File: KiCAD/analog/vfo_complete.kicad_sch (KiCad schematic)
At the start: 57 parts, among them J1 Filter Out, J10 Filter Out, J2 Filter Out, Q2 40673, U10 LM7171xIN, U11 LM7171xIN, U12 LM7171xIN, U5 Si5351A_Breakout

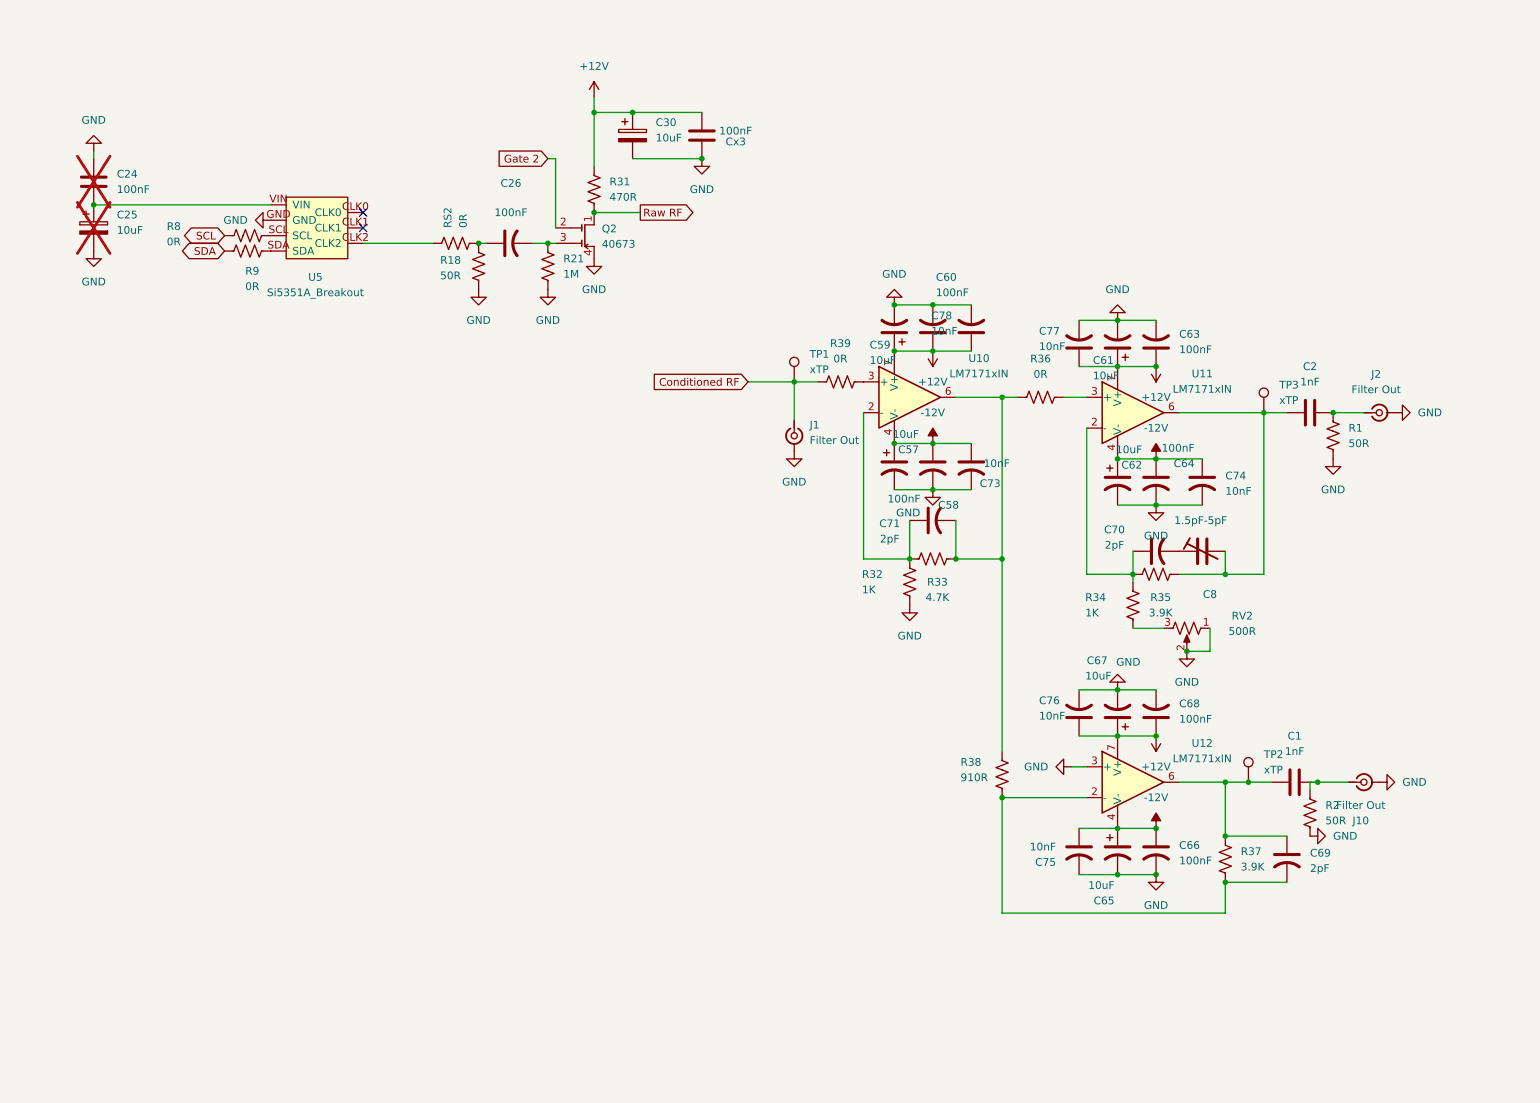
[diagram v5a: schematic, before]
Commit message: revD: analog board — DGFET+RC+buffer chain, LPF moved to ss_pa, PCB resized
Architecture change motivated by the Rev C sim finding that the LM7171
PP driver's +/-12V rails capped clean output at ~4.5W (see commit
3ce203d). Rev D delegates the gain-driver job to an external PA stage
(expected: QRP Labs 10W kit), so the analog board now just:
  Si5351 -> DGFET keyer -> R1(50)+C1(100p) RC @ 32MHz
         -> U1 LM7171 unity-gain follower -> R2(50) back-match -> J1 coax

Analog board changes (vfo_complete.kicad_sch):
  * DELETED: U10, U11, U12 (LM7171 PP driver chain) + feedback R/C,
    AC-coupling caps, V_BIAS network, R_GA/R_GB, C_GA/C_GB, J3/J4
    (dual-ended PP coax outputs)
  * DELETED: U2 reconstruction LPF stage (part of lpf.kicad_sch which
    is now emptied -- content moved to ss_pa/lpf.kicad_sch)
  * ADDED: R1=50R + C1=100pF (32 MHz single-pole RC snubber at the
    DGFET drain), U1 LM7171 unity-gain follower, R2=50R output
    back-match, J1 Conn_Coaxial_Small (new single-ended RF output),
    C2/C3=100nF op-amp bypass caps

Arduino sheet (arduino.kicad_sch):
  * ADDED: J2 Amphenol RJE1D-188 RJ45 for new external LPF board
    - Pins 1,2,3,6: RLY_10/15/17/20 band-select signals from PCF8575
    - Pins 5,8: GRID_CTL_A/B reserved spares for potential future
      tube PA (no other destination on the board, intentional)
    - Pins 4,7,SH: GND
  * ADDED: RLY_40 provision (not yet routed to J2, provision only)
  * T568B wire-pair arrangement for noise immunity

LPF content moved from analog/lpf.kicad_sch -> ss_pa/lpf.kicad_sch
(empty analog LPF sheet remains as a shell; delete later or repurpose).

PCB (analog.kicad_pcb):
  * Resized board outline from oversized 228x178 mm to 200x150 mm
    landscape (300 cm^2 / 46.5 in^2), centered on A3 at (210, 148.5)
  * Four M3 mounting holes H1-H4 placed 5 mm in from each corner
    (hole span 190 x 140 mm)
  * Added "board_only" attribute to each mounting hole so KiCad no
    longer flags them for deletion in Update PCB f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
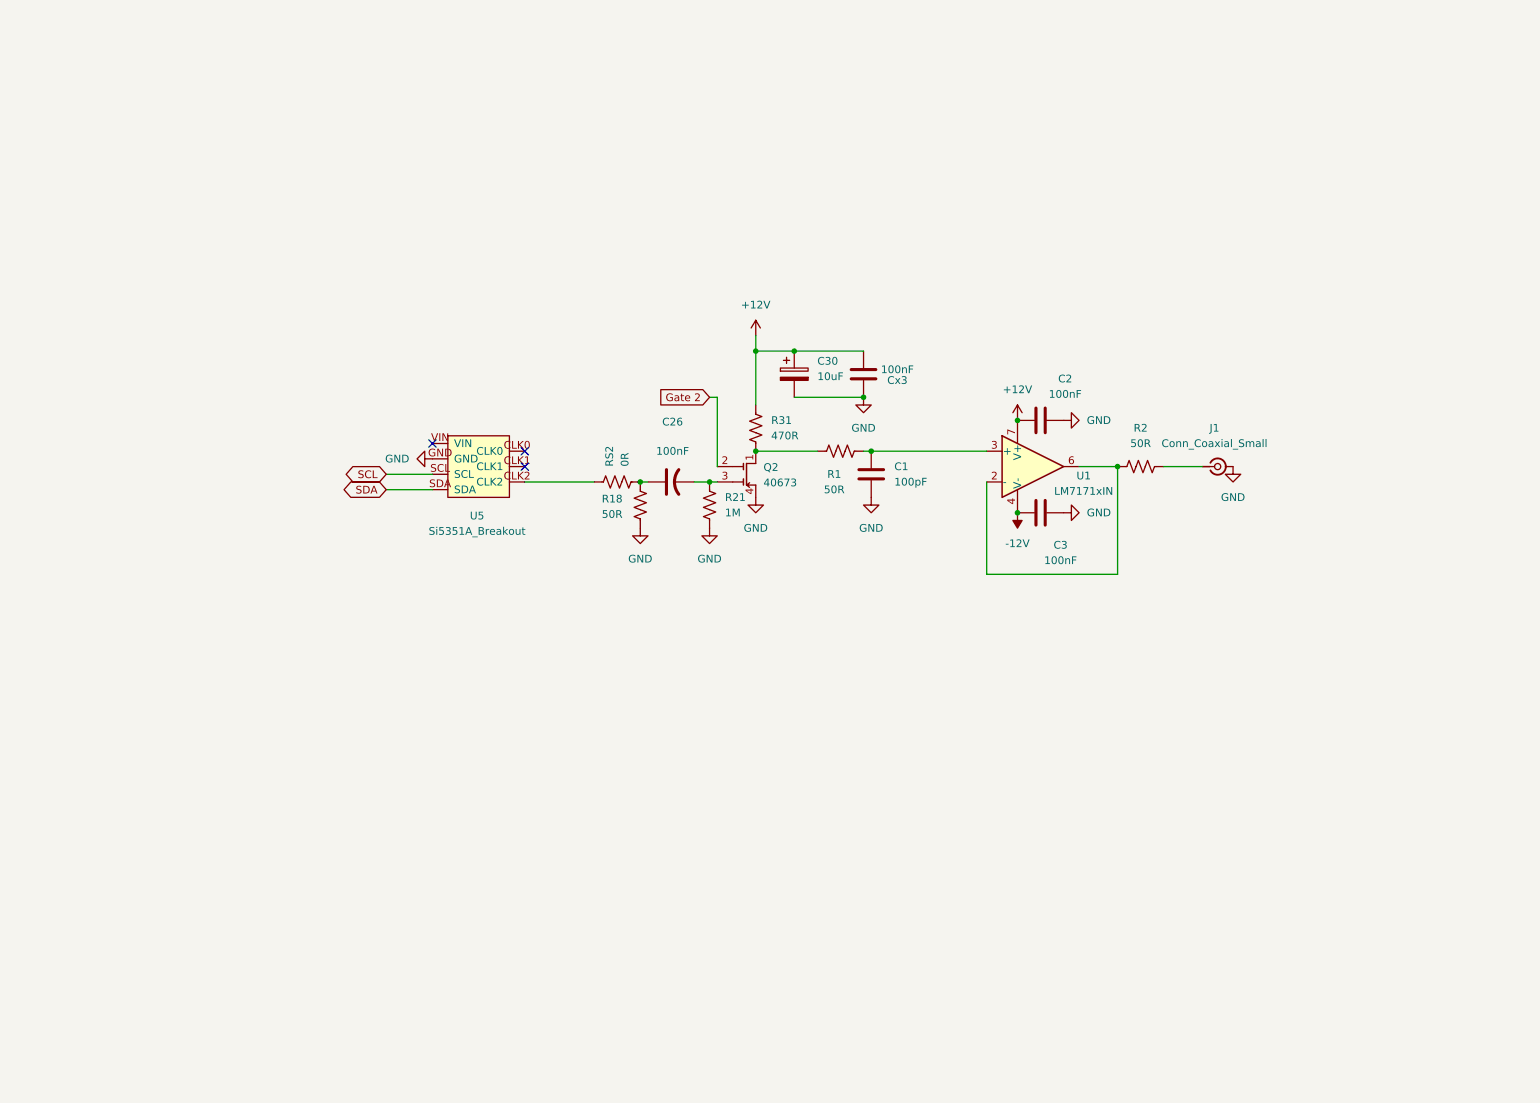
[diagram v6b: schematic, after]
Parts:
- removed C24: 100nF, Capacitor_THT:C_Disc_D5.0mm_W2.5mm_P5.00mm, symbol Device:C
- removed C25: 10uF, Capacitor_THT:CP_Radial_D5.0mm_P2.00mm, symbol Device:C_Polarized
- removed C57, C59, C61, C62, C65, C67: 10uF, Capacitor_THT:CP_Radial_D5.0mm_P2.00mm, symbol Device:C_Polarized_US
- removed C58, C60, C63, C64, C66, C68: 100nF, Capacitor_THT:C_Disc_D5.0mm_W2.5mm_P5.00mm, symbol Device:C_US
- removed C69, C70, C71: 2pF, xmitter:C_Axial_Kemet_Aximax_C41X_L4.5mm_D2.6mm_P7.62mm_Horizontal, symbol Device:C_US
- removed C73, C74, C75, C76, C77, C78: 10nF, Capacitor_THT:C_Disc_D6.0mm_W2.5mm_P5.00mm, symbol Device:C_US
- removed C8: 1.5pF-5pF, xmitter:Trimmer_Vishay_BFC2808_D5mm_P5.08mm, symbol Device:C_Trim
- removed J10, J2: Filter Out, Connector_Coaxial:SMA_Amphenol_132134_Vertical, symbol Connector:Conn_Coaxial_Small
- removed R32, R34: 1K, Resistor_THT:R_Axial_DIN0207_L6.3mm_D2.5mm_P10.16mm_Horizontal, symbol Device:R_US
- removed R33: 4.7K, Resistor_THT:R_Axial_DIN0207_L6.3mm_D2.5mm_P10.16mm_Horizontal, symbol Device:R_US
- removed R35, R37: 3.9K, Resistor_THT:R_Axial_DIN0207_L6.3mm_D2.5mm_P10.16mm_Horizontal, symbol Device:R_US
- removed R36, R39, R8, R9: 0R, Resistor_THT:R_Axial_DIN0207_L6.3mm_D2.5mm_P10.16mm_Horizontal, symbol Device:R_US
- removed R38: 910R, Resistor_THT:R_Axial_DIN0207_L6.3mm_D2.5mm_P10.16mm_Horizontal, symbol Device:R_US
- removed RV2: 500R, Potentiometer_THT:Potentiometer_Bourns_3296W_Vertical, symbol Device:R_Potentiometer_US
- removed TP1, TP2, TP3: xTP, Connector_PinHeader_2.54mm:PinHeader_1x01_P2.54mm_Vertical, symbol xmitter:xTP
- removed U10, U11, U12: LM7171xIN, Package_DIP:DIP-8_W7.62mm, symbol Amplifier_Operational:LM7171xIN
- added C3: 100nF, Capacitor_THT:C_Disc_D5.0mm_W2.5mm_P5.00mm, symbol Device:C
- added U1: LM7171xIN, Package_DIP:DIP-8_W7.62mm, symbol Amplifier_Operational:LM7171xIN
- C1: value 1nF -> 100pF
- C2: value 1nF -> 100nF; footprint Capacitor_THT:C_Rect_L7.0mm_W3.5mm_P5.00mm -> Capacitor_THT:C_Disc_D5.0mm_W2.5mm_P5.00mm
- J1: value Filter Out -> Conn_Coaxial_Small; footprint Connector_Coaxial:SMA_Amphenol_132134_Vertical -> xmitter:SMA_Cinch_142-0701-201_Vertical_JackPCB
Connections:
- net Raw RF is gone; now on an unnamed net: Q2.1 (D), R31.2
- net +12V: now also C2.1, U1.7 (V+)
- net -12V: now also C3.1, U1.4 (V-)
- net GND: now also C1.2, C2.2, C3.2; no longer R1.2, R2.2
- net SCL: now also U5.SCL
- net SDA: now also U5.SDA
- net at C1.1: now also R1.2, U1.3 (+)
- net at R2.1: now also U1.2 (-), U1.6; no longer C1.2
- net at R1.1: no longer C2.2
- net Conditioned RF: no longer names the net of J1.1 (In)
- net Conditioned RF: now also R2.2
- no-connect marks 2 -> 3
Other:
- moved on the sheet: C26, C30, Cx3, Q2, R18, R21, R31, RS2, U5

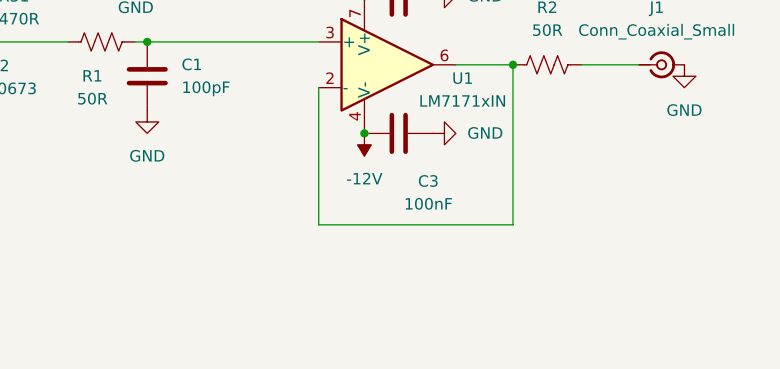
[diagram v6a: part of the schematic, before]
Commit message: revD analog: U1 gain hedge (R_f=3k installed, R_g unpopulated = unity default)
U1 (LM7171 buffer on analog) switched from unity-gain follower to a
non-inverting amplifier topology with a build-time gain hedge:

  - R_f = 3 kΩ installed in the feedback path (output -> inverting in)
  - R_g (inverting in -> GND) INTENTIONALLY LEFT UNPOPULATED by default

With R_g open, gain = 1 + R_f/R_g collapses to unity (nothing to force
current through R_f since LM7171 input bias is ~2 µA). Default signal
level at J1 is ~500 mVpp (unchanged from previous follower).

To get more drive at build time -- e.g. to push the IRF510 PA into
class-C operation when firmware sets PA_Bias_A/B low -- just populate
R_g with a value:
  R_g = 1 kΩ  -> gain = 4 -> ~2 Vpp into PA (comfortable, no clipping)
  R_g = 3 kΩ  -> gain = 2 -> ~1 Vpp
  R_g = 333 Ω -> gain = 10 -> clips, don't do

Amplitude control remains via Q2 (40673 DGFET) G2 driven by MCP4921
U4 ch A (envelope DAC via Q11/Q12 KeyUp mute level shifter). G2 acts
as a VCA; firmware applies CW envelope shaping (raised-cosine 5 ms).

Design rationale: relay-switched class-mode selection ruled out --
firmware control of PA_Bias_A/B (via MCP4728 U3) + DGFET G2 VCA
already covers both class-AB (full bias, moderate drive) and
class-C (low bias, high drive via populated R_g) without added
hardware.

Docs updated:
  * Documentation/revD_interconnect.md -- J1 section expanded to
    cover the gain hedge and amplitude-control architecture;
    change log entry added.

Co-Authored-By: Claude Opus 4.7 <noreply@anthropic.com>
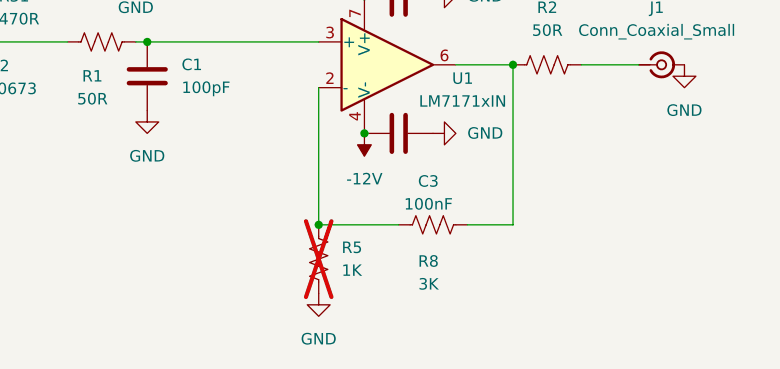
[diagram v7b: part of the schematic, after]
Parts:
- added R5: 1K, symbol Device:R_US
- added R8: 3K, symbol Device:R_US
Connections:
- net GND: now also R5.2
- net at R2.1, U1.6: now also R8.2; no longer U1.2 (-)
- new net: R5.1, R8.1, U1.2 (-)

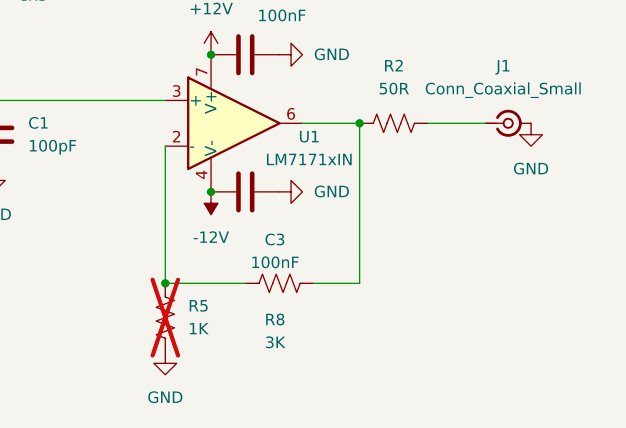
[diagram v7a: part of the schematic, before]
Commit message: revD analog: J23/J24 SMAs removed, many test points added, test_points.md
Schematic cleanup round:
  * Deleted J23 and J24 (SMAs that had carried GRID_CTL_A/B).
    These were redundant now that J35 is the production tube-PA
    control umbilical. Bench probing of GRID_CTL_A/B is now via
    TP2/TP1 (test-point pads) instead of SMA jacks.
  * Added 21 test points (TP1..TP21) across arduino, dac, and
    vfo_complete sheets. Covers:
      - Tube-PA control bus (TP1,2,5,6,7)
      - SS PA bias/sense/fault (TP3,4,12,13,14,15)
      - Keyer / envelope / U1 output (TP10,20,21)
      - DAC control lines (TP8,9)
      - Relay driver gates (TP11,16,17,18)
      - Hardware watchdog trigger (TP19)
    All on standard test-point pads for scope-probe or DMM access.

New doc: Documentation/test_points.md
  * Grouped TP table by functional area
  * Includes source/description for each signal
  * Includes a "how to use at the bench" section with common
    debug workflows (RF chain, bias setting, fault chain,
    future tube-PA bring-up, watchdog verification)
  * Uses monospace-aligned columns rather than markdown tables,
    per project convention for saved docs

Co-Authored-By: Claude Opus 4.7 <noreply@anthropic.com>
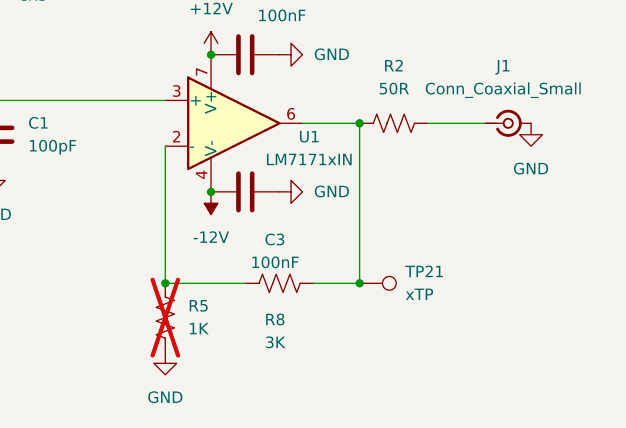
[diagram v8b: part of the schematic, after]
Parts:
- added TP21: xTP, Connector_PinHeader_2.54mm:PinHeader_1x01_P2.54mm_Vertical, symbol xmitter:xTP
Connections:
- net at R2.1, R8.2, U1.6: now also TP21.1
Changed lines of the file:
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@@
+	)
+	(junction
+		(at 194.31 105.41)
+		(diameter 0)
+		(color 0 0 0 0)
 	)
 	(junction
@@
 					(unit 1)
 				)
+			)
+		)
+	)
+	(symbol
+		(lib_id "xmitter:xTP")
+		(at 194.31 105.41 270)
+		(unit 1)
+		(body_style 1)
+		(exclude_from_sim no)
+		(in_bom yes)
+		(on_board yes)
+		(in_pos_files yes)
+		(dnp no)
+		(fields_autoplaced yes)
+		(property "Reference" "TP21"
+			(at 199.39 104.1399 90)
+			(show_name no)
+			(do_not_autoplace no)
+			(effects
+				(font
+					(size 1.27 1.27)
+				)
+				(justify left)
+			)
+		)
+		(property "Value" "xTP"
+			(at 199.39 106.6799 90)
+			(show_name no)
+			(do_not_autoplace no)
+			(effects
+				(font
+					(size 1.27 1.27)
+				)
+				(justify left)
+			)
+		)
+		(property "Footprint" "Connector_PinHeader_2.54mm:PinHeader_1x01_P2.54mm_Vertical"
+			(at 194.31 110.49 0)
+			(hide yes)
+			(show_name no)
+			(do_not_autoplace no)
+			(effects
+				(font
+					(size 1.27 1.27)
+				)
+			)
+		)
+		(property "Datasheet" ""
+			(at 194.31 110.49 0)
+			(hide yes)
+			(show_name no)
+			(do_not_autoplace no)
+			(effects
+				(font
+					(size 1.27 1.27)
+				)
+			)
+		)
+		(property "Description" "xmitter project test point on broken-off 0.1 inch square pin header; put signal name in Value field so it becomes silk on the PCB"
+			(at 194.31 105.41 0)
+			(hide yes)
+			(show_name no)
+			(do_not_autoplace no)
+			(effects
+				(font
+					(size 1.27 1.27)
+				)
+			)
+		)
+		(pin "1"
+		)
+		(instances
+			(project "analog"
+				(path "/d3de40b8-856b-4fbd-829c-f45ffcd55742/94bbc356-fa50-4d6f-b6f0-2ea7eca96dd3"
+					(reference "TP21")
+					(unit 1)
+				)
